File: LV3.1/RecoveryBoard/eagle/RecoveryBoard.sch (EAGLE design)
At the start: 92 parts, among them IC1 BD62120AEFJ-E2, Q1 BSS123, Q2 BSS123, Q3 BSS123, Q6 MOSFET-PCH-SOT23-6, U1 STM32F042K6, U10 TPS63070, Y1 ECS-160-10-36Q-ES-TR

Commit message: adding libraries to repo and notes from design review
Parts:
- C15: value 0.1uF -> 100nF
- R15: value 2636 -> 26.36K
- R16: value 1000 -> 10K
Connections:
- removed net N$8: IC1.OUT2, J2.2
- new net LAMOTOR+: IC1.OUT1, J2.1
- net GND: now also IC1.TEST
- net LAMOTOR-: now also IC1.OUT2, J2.2; no longer IC1.OUT1, J2.1
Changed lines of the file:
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@@
 <parts>
 <part name="U1" library="U-ST-STM32F042K-uC" deviceset="STM32F042K6" device=""/>
-<part name="SUPPLY2" library="supply2" library_urn="urn:adsk.eagle:library:372" deviceset="GND" device=""/>
 <part name="C1" library="oresat-rcl" deviceset="C-EU" device="0603-C-NOSILK" value="0.1uF"/>
 <part name="SUPPLY3" library="supply2" library_urn="urn:adsk.eagle:library:372" deviceset="GND" device=""/>
@@
 <part name="R14" library="oresat-rcl" deviceset="R-US_" device="0603-C-NOSILK" value="3.3K"/>
 <part name="P+4" library="supply1" library_urn="urn:adsk.eagle:library:371" deviceset="+12V" device=""/>
-<part name="R15" library="oresat-rcl" deviceset="R-US_" device="0603-C-NOSILK" value="2636">
+<part name="R15" library="oresat-rcl" deviceset="R-US_" device="0603-C-NOSILK" value="26.36K">
 <attribute name="DIS" value="Digi-Key"/>
 <attribute name="DPN" value="1276-4275-1-ND"/>
@@
 <attribute name="MPN" value="RC1005F6653CS"/>
 </part>
-<part name="R16" library="oresat-rcl" deviceset="R-US_" device="0603-C-NOSILK" value="1000">
+<part name="R16" library="oresat-rcl" deviceset="R-US_" device="0603-C-NOSILK" value="10K">
 <attribute name="DIS" value="Digi-Key"/>
 <attribute name="DPN" value="1276-4275-1-ND"/>
@@
 <part name="SUPPLY47" library="supply2" library_urn="urn:adsk.eagle:library:372" deviceset="GND" device=""/>
 <part name="U$8" library="Q--Si7465DP--Vishay Power MOSFET with multple S+D leads" deviceset="SI7465DP" device=""/>
-<part name="C15" library="oresat-rcl" deviceset="C-EU" device="0603-C-NOSILK" value="0.1uF"/>
+<part name="C15" library="oresat-rcl" deviceset="C-EU" device="0603-C-NOSILK" value="100nF"/>
 <part name="C14" library="oresat-rcl" deviceset="C-EU" device="0603-C-NOSILK" value="0.1uF"/>
 <part name="R20" library="oresat-rcl" deviceset="R-US_" device="0603-C-NOSILK"/>
@@
 </part>
 <part name="IC1" library="SamacSys_Parts" deviceset="BD62120AEFJ-E2" device=""/>
+<part name="SUPPLY1" library="supply2" library_urn="urn:adsk.eagle:library:372" deviceset="GND" device=""/>
 </parts>
 <sheets>
@@
 <attribute name="VALUE" x="287.02" y="154.94" size="1.778" layer="96"/>
 </instance>
-<instance part="SUPPLY2" gate="GND" x="499.11" y="143.51" smashed="yes"/>
 <instance part="C1" gate="CE" x="451.485" y="170.815" smashed="yes">
 <attribute name="NAME" x="453.009" y="171.196" size="1.778" layer="95"/>
@@
 <attribute name="VALUE" x="480.06" y="166.37" size="1.778" layer="96" align="center-left"/>
 </instance>
+<instance part="SUPPLY1" gate="GND" x="443.865" y="140.335" smashed="yes"/>
 </instances>
 <busses>
@@
 <pinref part="SUPPLY42" gate="GND" pin="GND"/>
 <pinref part="Q3" gate="G$1" pin="S"/>
+</segment>
+<segment>
+<pinref part="IC1" gate="G$1" pin="TEST"/>
+<wire x1="453.39" y1="158.75" x2="443.865" y2="158.75" width="0.1524" layer="91"/>
+<wire x1="443.865" y1="158.75" x2="443.865" y2="142.875" width="0.1524" layer="91"/>
+<pinref part="SUPPLY1" gate="GND" pin="GND"/>
 </segment>
 </net>
@@
 </segment>
 </net>
-<net name="LAMOTOR-" class="0">
+<net name="LAMOTOR+" class="0">
 <segment>
 <wire x1="497.84" y1="158.75" x2="497.84" y2="215.9" width="0.1524" layer="91"/>
@@
 </segment>
 </net>
-<net name="N$8" class="0">
+<net name="LAMOTOR-" class="0">
 <segment>
 <pinref part="J2" gate="A" pin="2"/>
@@
 <wire x1="501.015" y1="156.21" x2="483.87" y2="156.21" width="0.1524" layer="91"/>
 <wire x1="501.015" y1="213.36" x2="501.015" y2="156.21" width="0.1524" layer="91"/>
-</segment>
-</net>
+<label x="502.92" y="179.07" size="1.778" layer="95" rot="R90"/>
+</segment>
+</net>

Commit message: implementing design changes from 1/21/2020
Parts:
- removed SENSOR, SENSOR2: BPR-301, BPR-301:BPR-301
- added JP3: (no value), pinhead:PINHD-1X3
- added Q4, Q5: BPR-301, Q--BPR-301--Phototransistor:BPR-301
- added TP1, TP2, TP3, TP4: TEST-POINT, Tova:TEST-POINT
- C1, C14: value 0.1uF -> 100n
- C11, C12, C21: value 10uF -> 10u
- C13: value 0.1uF -> 0.1u
- C15: value 100nF -> 100n
- C16: value 2.2nF -> 2.2n
- C17: value 22uF -> 22u
- C22: value 100uF -> 100n
- C3, C4: value 20pF -> 20p
- R27: value TBD -> 50
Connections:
- net 3.3V: now also Q4.ANOD, Q4.COLL, Q5.ANOD, Q5.COLL; no longer SENSOR.ANOD, SENSOR.COLL, SENSOR2.ANOD, SENSOR2.COLL
- net CAN_RX: now also TP1.1
- net CAN_TX: now also TP2.1
- net GND: now also JP3.3
- net N$2: now also Q4.CATH; no longer SENSOR.CATH
- net N$5: now also Q5.CATH; no longer SENSOR2.CATH
- net SENSOR1: now also Q4.EMIT; no longer SENSOR.EMIT
- net SENSOR2: now also Q5.EMIT; no longer SENSOR2.EMIT
- net USART2_RX: now also JP3.1, TP3.1
- net USART2_TX: now also JP3.2, TP4.1
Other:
- note added: "USART Connector for Laptop"
- moved on the sheet: R32, R33

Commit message: created BOM
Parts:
- C17: value 22u -> 22uF
- R13: value 1.7K -> 1.69K
- R15: value 26.36K -> 26.4K
- R26, R27: value 50 -> 51.1
- R28: value 50 -> 10K
- R8, R9: value 439 -> 442
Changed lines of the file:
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@@
 <part name="SUPPLY4" library="supply2" library_urn="urn:adsk.eagle:library:372" deviceset="GND" device=""/>
 <part name="R7" library="oresat-rcl" deviceset="R-US_" device="0603-C-NOSILK" value="10K"/>
-<part name="R8" library="oresat-rcl" deviceset="R-US_" device="0603-C-NOSILK" value="439"/>
-<part name="R9" library="oresat-rcl" deviceset="R-US_" device="0603-C-NOSILK" value="439"/>
+<part name="R8" library="oresat-rcl" deviceset="R-US_" device="0603-C-NOSILK" value="442"/>
+<part name="R9" library="oresat-rcl" deviceset="R-US_" device="0603-C-NOSILK" value="442"/>
 <part name="R10" library="oresat-rcl" deviceset="R-US_" device="0603-C-NOSILK" value="10K"/>
 <part name="SUPPLY24" library="supply2" library_urn="urn:adsk.eagle:library:372" deviceset="GND" device=""/>
@@
 <part name="SUPPLY8" library="supply2" library_urn="urn:adsk.eagle:library:372" deviceset="GND" device=""/>
 <part name="SUPPLY9" library="supply2" library_urn="urn:adsk.eagle:library:372" deviceset="GND" device=""/>
-<part name="R13" library="oresat-rcl" deviceset="R-US_" device="0603-C-NOSILK" value="1.7K"/>
+<part name="R13" library="oresat-rcl" deviceset="R-US_" device="0603-C-NOSILK" value="1.69K"/>
 <part name="R14" library="oresat-rcl" deviceset="R-US_" device="0603-C-NOSILK" value="3.3K"/>
 <part name="P+4" library="supply1" library_urn="urn:adsk.eagle:library:371" deviceset="+12V" device=""/>
-<part name="R15" library="oresat-rcl" deviceset="R-US_" device="0603-C-NOSILK" value="26.36K">
+<part name="R15" library="oresat-rcl" deviceset="R-US_" device="0603-C-NOSILK" value="26.4K">
 <attribute name="DIS" value="Digi-Key"/>
 <attribute name="DPN" value="1276-4275-1-ND"/>
@@
 <part name="L2" library="L-Coilcraft-XFL4020" deviceset="L-COILCRAFT-XFL4020" device=""/>
 <part name="R22" library="oresat-rcl" deviceset="R-US_" device="1206-C" value="100m"/>
-<part name="C17" library="oresat-rcl" deviceset="C-EU" device="0805-C-NOSILK" value="22u"/>
+<part name="C17" library="oresat-rcl" deviceset="C-EU" device="0805-C-NOSILK" value="22uF"/>
 <part name="SUPPLY18" library="supply2" library_urn="urn:adsk.eagle:library:372" deviceset="GND" device=""/>
 <part name="U$7" library="SPK--SMT-0440-S-R--Speaker" deviceset="SMT-0440-S-R" device=""/>
@@
 <part name="SUPPLY23" library="supply2" library_urn="urn:adsk.eagle:library:372" deviceset="GND" device=""/>
 <part name="SUPPLY5" library="SparkFun-PowerSymbols" library_urn="urn:adsk.eagle:library:530" deviceset="3.3V" device=""/>
-<part name="R26" library="oresat-rcl" deviceset="R-US_" device="0603-C-NOSILK" value="50"/>
-<part name="R27" library="oresat-rcl" deviceset="R-US_" device="0603-C-NOSILK" value="50"/>
-<part name="R28" library="oresat-rcl" deviceset="R-US_" device="0603-C-NOSILK" value="50"/>
+<part name="R26" library="oresat-rcl" deviceset="R-US_" device="0603-C-NOSILK" value="51.1"/>
+<part name="R27" library="oresat-rcl" deviceset="R-US_" device="0603-C-NOSILK" value="51.1"/>
+<part name="R28" library="oresat-rcl" deviceset="R-US_" device="0603-C-NOSILK" value="10K"/>
 <part name="R29" library="oresat-rcl" deviceset="R-US_" device="0603-C-NOSILK" value="10k"/>
 <part name="SUPPLY34" library="supply2" library_urn="urn:adsk.eagle:library:372" deviceset="GND" device=""/>

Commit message: completed BOM except for a couple pin head connectors
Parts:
- removed R6: NP, oresat-rcl:R-US_0603-C-NOSILK
- C13: value 0.1u -> 100n
- L1: value 1.5 uH -> 1.5uH; device L-Coilcraft-XFL4020:L-COILCRAFT-XFL4020 -> L--IHLP2020CZER1R5M11--1.5uHInductor:IHLP2020CZER1R5M11; DIS Mouser -> (none); DPN 994-XFL4020-152MEB -> (none); MFR Coilcraft -> (none); MPN XFL4020-152ME -> (none)
- L2: value L-COILCRAFT-XFL4020 -> 4.7uH; device L-Coilcraft-XFL4020:L-COILCRAFT-XFL4020 -> L--IHLP2020BZER4R7M11--4.7uInductor:IHLP2020BZER4R7M11
- R10, R16, R28, R32, R33, R34, R35, R36, R7: value 10K -> 10k
- R11, R12: value 1K -> 1k
- R13: value 1.69K -> 1.69k
- R14: value 3.3K -> 3.3k
- R15: value 26.4K -> 26.4k
- R17: value (none) -> 10k
- R20: value (none) -> 2.4k
- R3: value 150K -> 150k
- R5: value NP -> 100k
- renumbered IC1 to U2
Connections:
- new net N$3: U2.TEST
- net GND: no longer R6.1, U2.TEST
- net N$10: now also L2.P$1; no longer L2.1
- net N$28: now also L2.P$2; no longer L2.2
- net TPS-EN: no longer R6.2
- net TPS-L1: now also L1.P$1; no longer L1.1
- net TPS-L2: now also L1.P$2; no longer L1.2

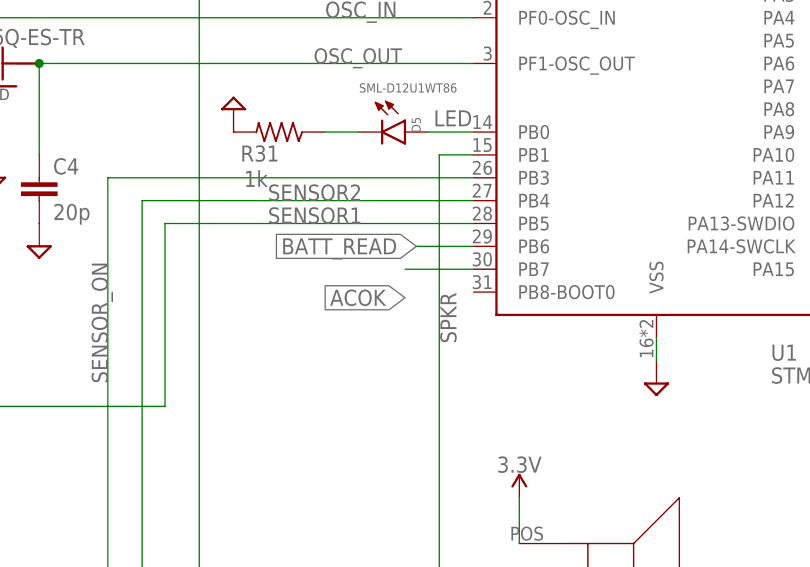
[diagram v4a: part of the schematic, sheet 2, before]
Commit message: finished bom without jtag and connectors
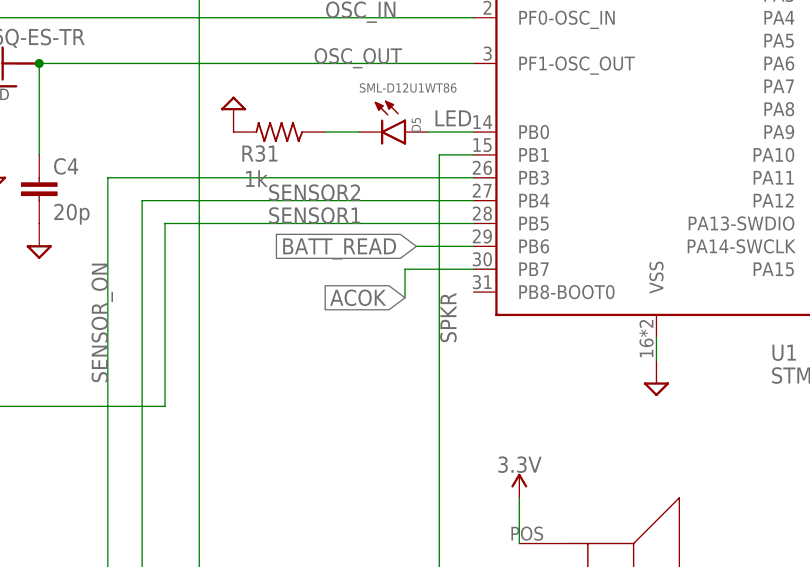
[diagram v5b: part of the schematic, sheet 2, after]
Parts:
- R2, R5: device oresat-rcl:R-US_0603-C-NOSILK -> oresat-rcl:R-US_0805-A-NOSILK
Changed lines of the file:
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@@
 </part>
 <part name="GND34" library="supply1" deviceset="GND" device=""/>
-<part name="R2" library="oresat-rcl" deviceset="R-US_" device="0603-C-NOSILK" value="470k">
+<part name="R2" library="oresat-rcl" deviceset="R-US_" device="0805-A-NOSILK" value="470k">
 <attribute name="DIS" value="Digi-Key"/>
 <attribute name="DPN" value="1276-4275-1-ND"/>
@@
 <part name="GND26" library="supply1" deviceset="GND" device=""/>
 <part name="TP29" library="Tova" deviceset="TEST-POINT" device=""/>
-<part name="R5" library="oresat-rcl" deviceset="R-US_" device="0603-C-NOSILK" value="100k">
+<part name="R5" library="oresat-rcl" deviceset="R-US_" device="0805-A-NOSILK" value="100k">
 <attribute name="DIS" value="Digi-Key"/>
 <attribute name="DPN" value="1276-4275-1-ND"/>
@@
 <wire x1="254" y1="167.64" x2="246.38" y2="167.64" width="0.1524" layer="91"/>
 <label x="246.38" y="164.465" size="1.778" layer="95" rot="R180" xref="yes"/>
-</segment>
-</net>
+<wire x1="246.38" y1="167.64" x2="246.38" y2="164.465" width="0.1524" layer="91"/>
+</segment>
+</net>
